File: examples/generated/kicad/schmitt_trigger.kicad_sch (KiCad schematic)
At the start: 7 parts

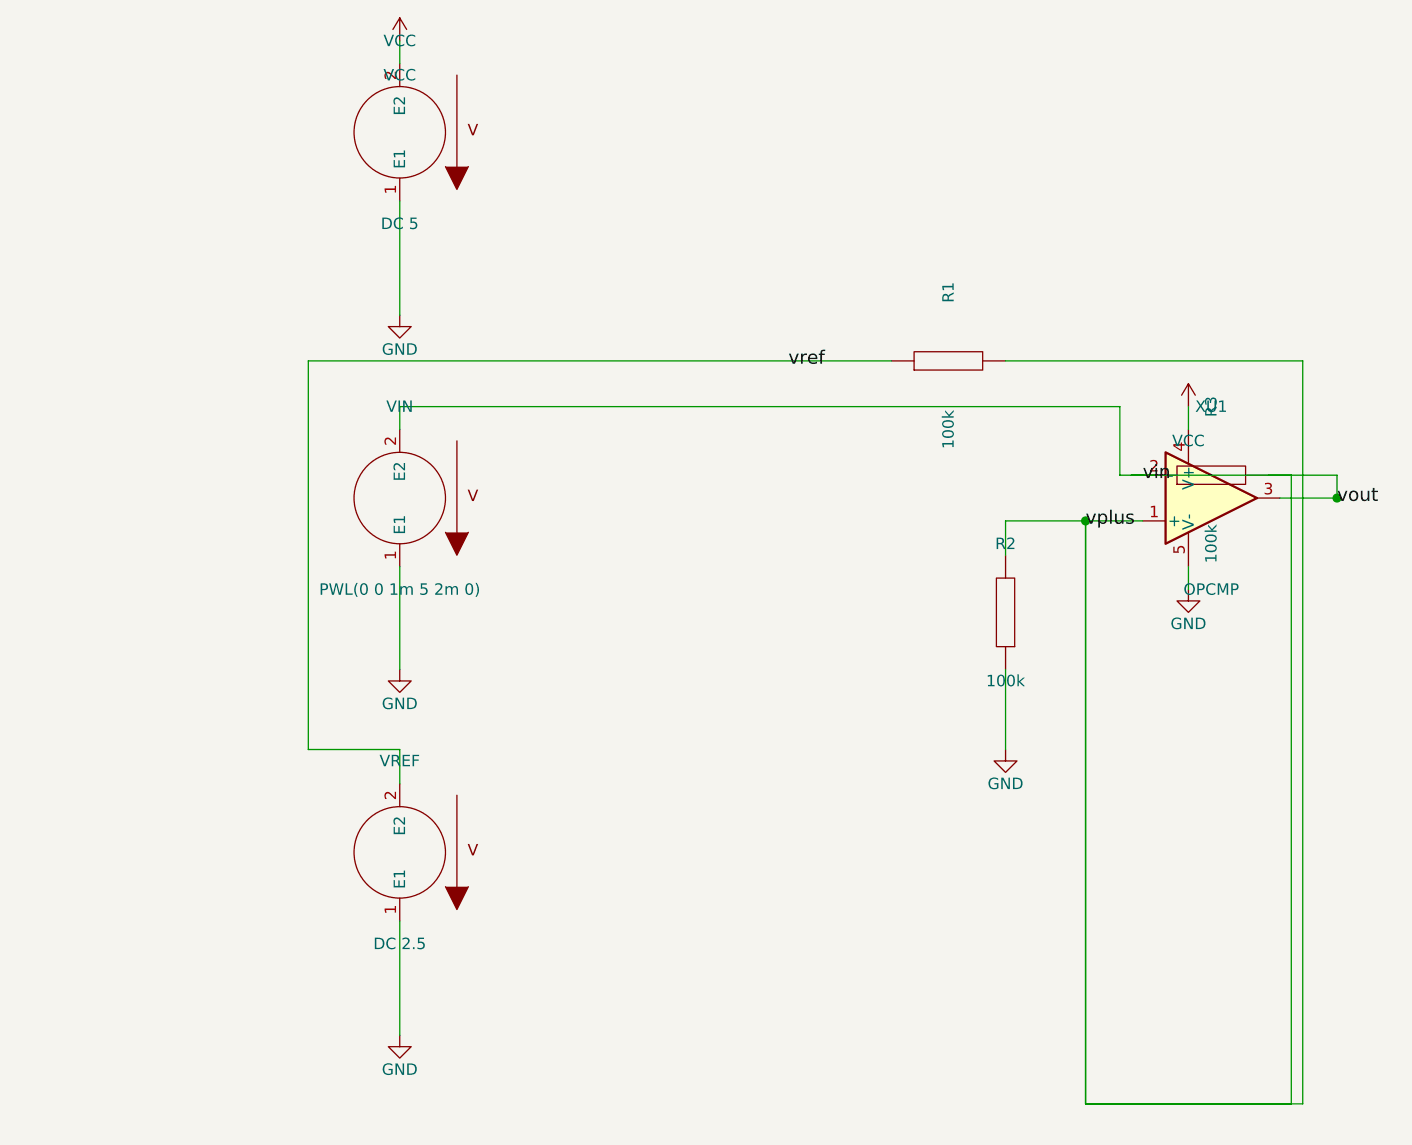
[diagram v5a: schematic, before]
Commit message: Fix CMOS inverter issue.
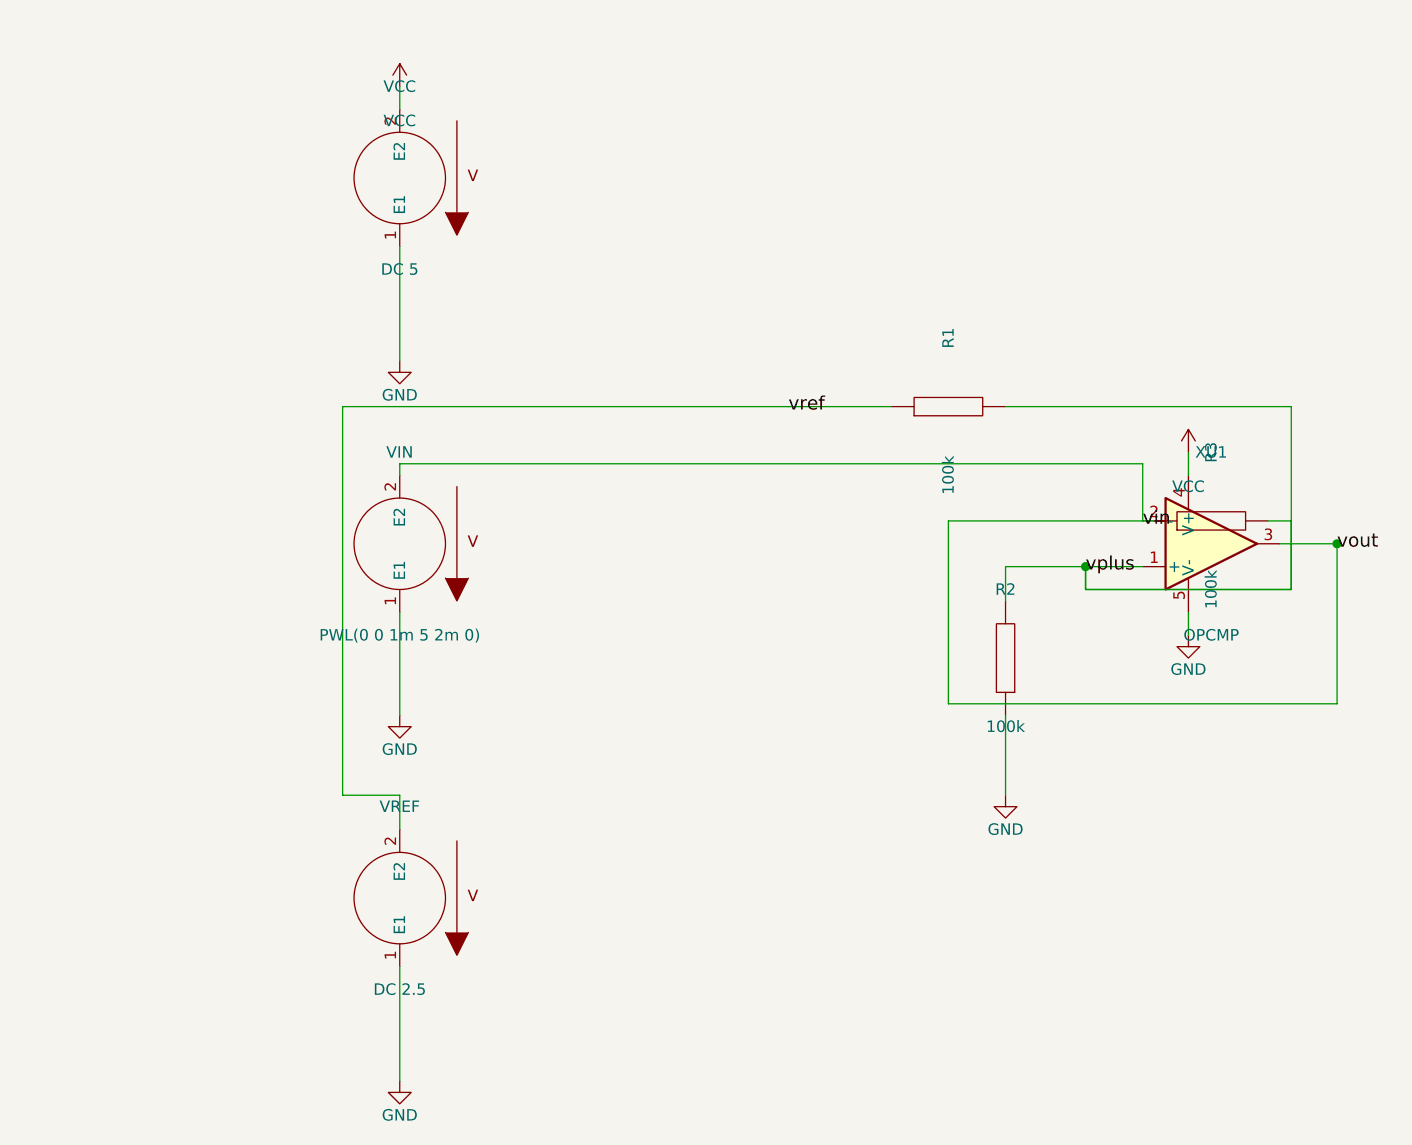
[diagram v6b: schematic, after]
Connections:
- net vin: no longer R1.2, R2.2, R3.2, XU1.1 (+)
- new net vplus: R1.2, R2.2, R3.2, XU1.1 (+)
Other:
- moved on the sheet: R1, R2, R3, VCC, VIN, VREF, XU1

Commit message: Attempt to fix scmitt trigger connectivity and wiring.
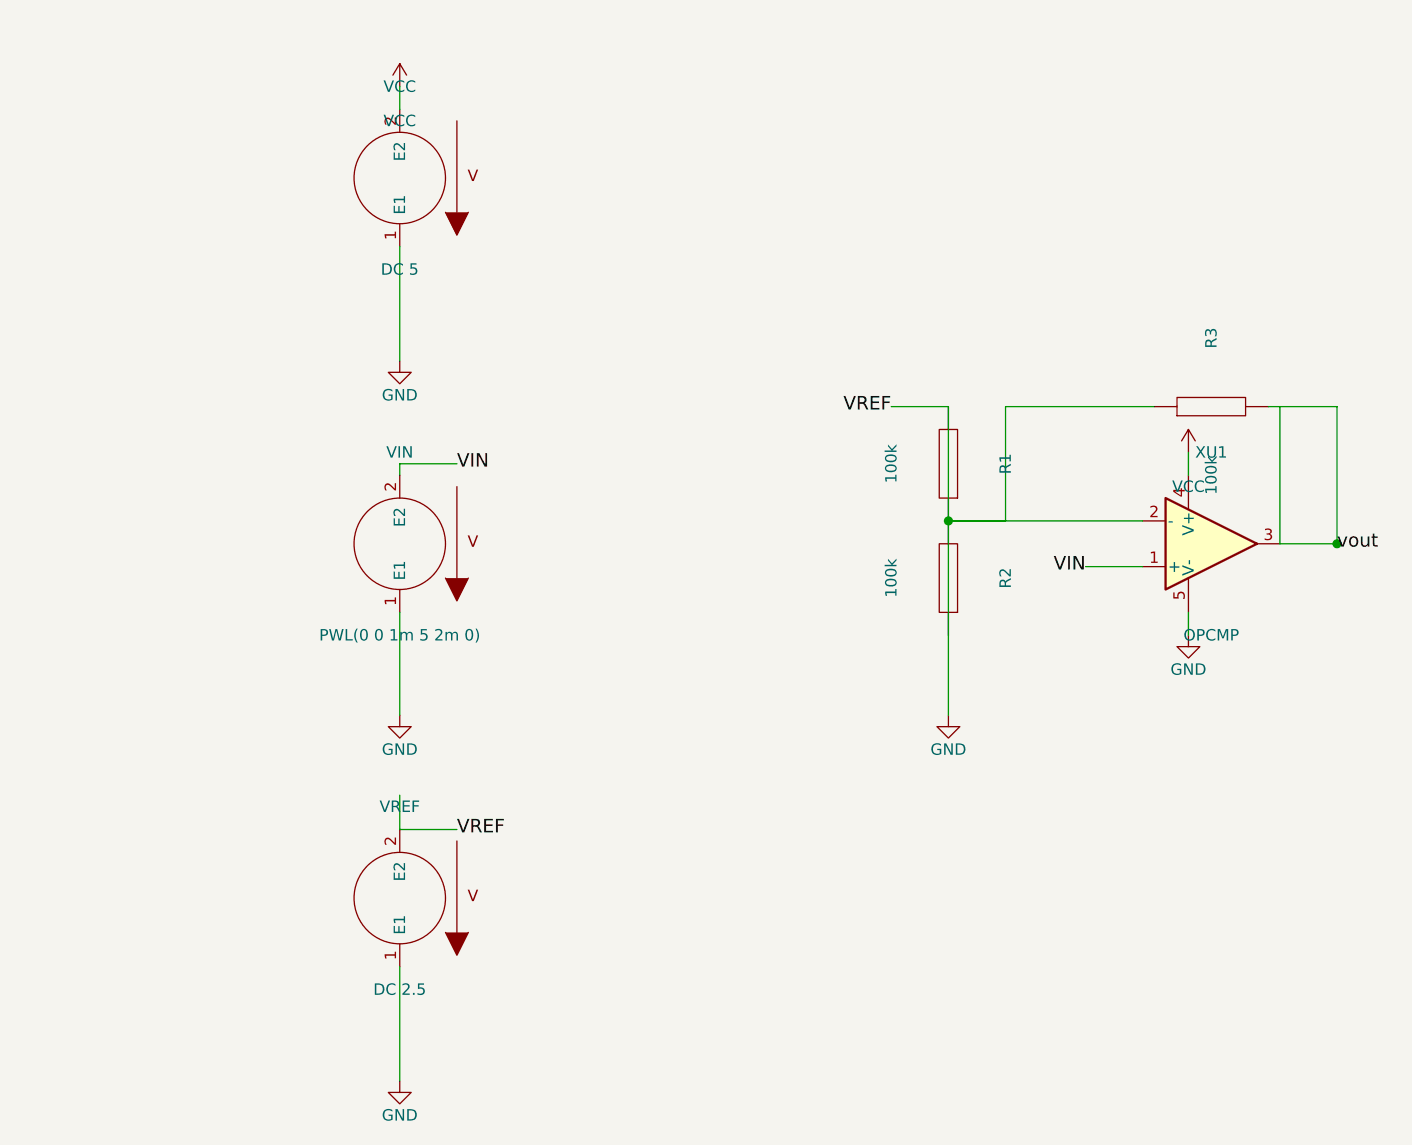
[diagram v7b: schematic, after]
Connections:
- net vref is gone; now on net GND: R1.1, VREF.2 (E2)
- net GND: now also R1.2, R2.2, R3.1, XU1.2 (-)
- removed net vin: R3.1, VIN.2 (E2), XU1.2 (-), XU1.3
- removed net vplus: R1.2, R2.2, R3.2, XU1.1 (+)
- new net VIN: VIN.2 (E2), XU1.1 (+)
- new net vout: R3.2, XU1.3
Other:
- moved on the sheet: R1, R2, R3
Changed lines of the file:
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@@
     )
   )
-  (symbol (lib_id "R") (at 140.97 85.09 90) (unit 1)
-    (in_bom yes) (on_board yes)
-    (property "Reference" "R1" (at 140.97 77.47 0)
-      (effects (font (size 1.27 1.27)))
-    )
-    (property "Value" "100k" (at 140.97 92.71 0)
-      (effects (font (size 1.27 1.27)))
-    )
-    (property "Footprint" "" (at 0 0 0)
-      (effects (font (size 1.27 1.27)) hide)
-    )
-    (property "Datasheet" "" (at 0 0 0)
-      (effects (font (size 1.27 1.27)) hide)
-    )
-  )
-  (symbol (lib_id "R") (at 147.32 113.03 180) (unit 1)
-    (in_bom yes) (on_board yes)
-    (property "Reference" "R2" (at 147.32 105.41 0)
-      (effects (font (size 1.27 1.27)))
-    )
-    (property "Value" "100k" (at 147.32 120.65 0)
-      (effects (font (size 1.27 1.27)))
-    )
-    (property "Footprint" "" (at 0 0 0)
-      (effects (font (size 1.27 1.27)) hide)
-    )
-    (property "Datasheet" "" (at 0 0 0)
-      (effects (font (size 1.27 1.27)) hide)
-    )
-  )
-  (symbol (lib_id "R") (at 170.18 97.79 90) (unit 1)
-    (in_bom yes) (on_board yes)
-    (property "Reference" "R3" (at 170.18 90.17 0)
-      (effects (font (size 1.27 1.27)))
-    )
-    (property "Value" "100k" (at 170.18 105.41 0)
+  (symbol (lib_id "R") (at 140.97 91.44 180) (unit 1)
+    (in_bom yes) (on_board yes)
+    (property "Reference" "R1" (at 147.32 91.44 90)
+      (effects (font (size 1.27 1.27)))
+    )
+    (property "Value" "100k" (at 134.62 91.44 90)
+      (effects (font (size 1.27 1.27)))
+    )
+    (property "Footprint" "" (at 0 0 0)
+      (effects (font (size 1.27 1.27)) hide)
+    )
+    (property "Datasheet" "" (at 0 0 0)
+      (effects (font (size 1.27 1.27)) hide)
+    )
+  )
+  (symbol (lib_id "R") (at 140.97 104.14 180) (unit 1)
+    (in_bom yes) (on_board yes)
+    (property "Reference" "R2" (at 147.32 104.14 90)
+      (effects (font (size 1.27 1.27)))
+    )
+    (property "Value" "100k" (at 134.62 104.14 90)
+      (effects (font (size 1.27 1.27)))
+    )
+    (property "Footprint" "" (at 0 0 0)
+      (effects (font (size 1.27 1.27)) hide)
+    )
+    (property "Datasheet" "" (at 0 0 0)
+      (effects (font (size 1.27 1.27)) hide)
+    )
+  )
+  (symbol (lib_id "R") (at 170.18 85.09 90) (unit 1)
+    (in_bom yes) (on_board yes)
+    (property "Reference" "R3" (at 170.18 77.47 0)
+      (effects (font (size 1.27 1.27)))
+    )
+    (property "Value" "100k" (at 170.18 92.71 0)
       (effects (font (size 1.27 1.27)))
     )
@@
     )
   )
-  (symbol (lib_id "GND") (at 147.32 128.27 0) (unit 1)
-    (in_bom yes) (on_board yes)
-    (property "Reference" "#PWR0001" (at 147.32 124.46000000000001 0)
-      (effects (font (size 1.27 1.27)) hide)
-    )
-    (property "Value" "GND" (at 147.32 132.08 0)
+  (symbol (lib_id "GND") (at 140.97 119.38 0) (unit 1)
+    (in_bom yes) (on_board yes)
+    (property "Reference" "#PWR0001" (at 140.97 115.57 0)
+      (effects (font (size 1.27 1.27)) hide)
+    )
+    (property "Value" "GND" (at 140.97 123.19 0)
       (effects (font (size 1.27 1.27)))
     )
@@
     )
   )
-  (label "vin" (at 162.56 97.79 0)
-    (effects (font (size 1.50 1.50)))
-  )
-  (label "vref" (at 123.19 85.09 0)
-    (effects (font (size 1.50 1.50)))
-  )
-  (label "vplus" (at 156.21 102.87 0)
+  (label "VIN" (at 86.36 91.44 0)
+    (effects (font (size 1.50 1.50)))
+  )
+  (label "VREF" (at 86.36 132.08 0)
+    (effects (font (size 1.50 1.50)))
+  )
+  (label "VIN" (at 156.21 102.87 180)
+    (effects (font (size 1.50 1.50)))
+  )
+  (label "VREF" (at 134.62 85.09 180)
     (effects (font (size 1.50 1.50)))
   )
@@
     (stroke (width 0) (type solid) (color 0 0 0 0))
   )
-  (wire (pts (xy 80.01 91.44) (xy 162.56 91.44))
-    (stroke (width 0) (type solid) (color 0 0 0 0))
-  )
-  (wire (pts (xy 162.56 91.44) (xy 162.56 97.79))
+  (wire (pts (xy 80.01 132.08) (xy 86.36 132.08))
+    (stroke (width 0) (type solid) (color 0 0 0 0))
+  )
+  (wire (pts (xy 156.21 102.87) (xy 162.56 102.87))
     (stroke (width 0) (type solid) (color 0 0 0 0))
   )
@@
     (stroke (width 0) (type solid) (color 0 0 0 0))
   )
-  (wire (pts (xy 80.01 128.27) (xy 73.66 128.27))
-    (stroke (width 0) (type solid) (color 0 0 0 0))
-  )
-  (wire (pts (xy 73.66 128.27) (xy 73.66 85.09))
-    (stroke (width 0) (type solid) (color 0 0 0 0))
-  )
-  (wire (pts (xy 73.66 85.09) (xy 123.19 85.09))
-    (stroke (width 0) (type solid) (color 0 0 0 0))
-  )
-  (wire (pts (xy 134.62 85.09) (xy 123.19 85.09))
-    (stroke (width 0) (type solid) (color 0 0 0 0))
-  )
-  (wire (pts (xy 147.32 85.09) (xy 179.07 85.09))
-    (stroke (width 0) (type solid) (color 0 0 0 0))
-  )
-  (wire (pts (xy 179.07 85.09) (xy 179.07 105.41))
-    (stroke (width 0) (type solid) (color 0 0 0 0))
-  )
-  (wire (pts (xy 179.07 105.41) (xy 156.21 105.41))
-    (stroke (width 0) (type solid) (color 0 0 0 0))
-  )
-  (wire (pts (xy 156.21 105.41) (xy 156.21 102.87))
-    (stroke (width 0) (type solid) (color 0 0 0 0))
-  )
-  (wire (pts (xy 147.32 106.68) (xy 147.32 102.87))
-    (stroke (width 0) (type solid) (color 0 0 0 0))
-  )
-  (wire (pts (xy 147.32 102.87) (xy 156.21 102.87))
-    (stroke (width 0) (type solid) (color 0 0 0 0))
-  )
-  (wire (pts (xy 176.53 97.79) (xy 179.07 97.79))
-    (stroke (width 0) (type solid) (color 0 0 0 0))
-  )
-  (wire (pts (xy 179.07 97.79) (xy 179.07 105.41))
-    (stroke (width 0) (type solid) (color 0 0 0 0))
-  )
-  (wire (pts (xy 179.07 105.41) (xy 156.21 105.41))
-    (stroke (width 0) (type solid) (color 0 0 0 0))
-  )
-  (wire (pts (xy 156.21 105.41) (xy 156.21 102.87))
-    (stroke (width 0) (type solid) (color 0 0 0 0))
-  )
-  (wire (pts (xy 162.56 102.87) (xy 156.21 102.87))
-    (stroke (width 0) (type solid) (color 0 0 0 0))
-  )
-  (wire (pts (xy 147.32 119.38) (xy 147.32 128.27))
+  (wire (pts (xy 140.97 110.49) (xy 140.97 119.38))
+    (stroke (width 0) (type solid) (color 0 0 0 0))
+  )
+  (wire (pts (xy 134.62 85.09) (xy 140.97 85.09))
+    (stroke (width 0) (type solid) (color 0 0 0 0))
+  )
+  (wire (pts (xy 140.97 97.79) (xy 162.56 97.79))
+    (stroke (width 0) (type solid) (color 0 0 0 0))
+  )
+  (wire (pts (xy 140.97 97.79) (xy 140.97 110.49))
+    (stroke (width 0) (type solid) (color 0 0 0 0))
+  )
+  (wire (pts (xy 176.53 85.09) (xy 184.15 85.09))
+    (stroke (width 0) (type solid) (color 0 0 0 0))
+  )
+  (wire (pts (xy 184.15 85.09) (xy 184.15 100.33))
+    (stroke (width 0) (type solid) (color 0 0 0 0))
+  )
+  (wire (pts (xy 163.83 85.09) (xy 147.32 85.09))
+    (stroke (width 0) (type solid) (color 0 0 0 0))
+  )
+  (wire (pts (xy 147.32 85.09) (xy 147.32 97.79))
+    (stroke (width 0) (type solid) (color 0 0 0 0))
+  )
+  (wire (pts (xy 147.32 97.79) (xy 140.97 97.79))
+    (stroke (width 0) (type solid) (color 0 0 0 0))
+  )
+  (wire (pts (xy 80.01 91.44) (xy 86.36 91.44))
+    (stroke (width 0) (type solid) (color 0 0 0 0))
+  )
+  (wire (pts (xy 140.97 85.09) (xy 140.97 97.79))
     (stroke (width 0) (type solid) (color 0 0 0 0))
   )
@@
     (stroke (width 0) (type solid) (color 0 0 0 0))
   )
-  (wire (pts (xy 163.83 97.79) (xy 140.97 97.79))
-    (stroke (width 0) (type solid) (color 0 0 0 0))
-  )
-  (wire (pts (xy 140.97 97.79) (xy 140.97 118.11))
-    (stroke (width 0) (type solid) (color 0 0 0 0))
-  )
-  (wire (pts (xy 140.97 118.11) (xy 184.15 118.11))
-    (stroke (width 0) (type solid) (color 0 0 0 0))
-  )
-  (wire (pts (xy 184.15 118.11) (xy 184.15 100.33))
-    (stroke (width 0) (type solid) (color 0 0 0 0))
-  )
-  (junction (at 156.21 102.87) (diameter 1.016) (color 0 0 0 0))
+  (wire (pts (xy 177.80 100.33) (xy 177.80 85.09))
+    (stroke (width 0) (type solid) (color 0 0 0 0))
+  )
+  (junction (at 140.97 97.79) (diameter 1.016) (color 0 0 0 0))
   (junction (at 184.15 100.33) (diameter 1.016) (color 0 0 0 0))
   (sheet_instances
